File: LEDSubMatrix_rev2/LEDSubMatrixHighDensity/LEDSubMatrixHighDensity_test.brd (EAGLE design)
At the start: 16.9 x 146 mm, 145 parts, among them IC1 TLC5955DCAR, IC2 TLC5955DCAR, IC3 TLC5955DCAR, IC4 TLC5955DCAR, IC5 TLC5955DCAR, IC6 TLC5955DCAR, IC7 TLC5955DCAR, IC8 TLC5955DCAR

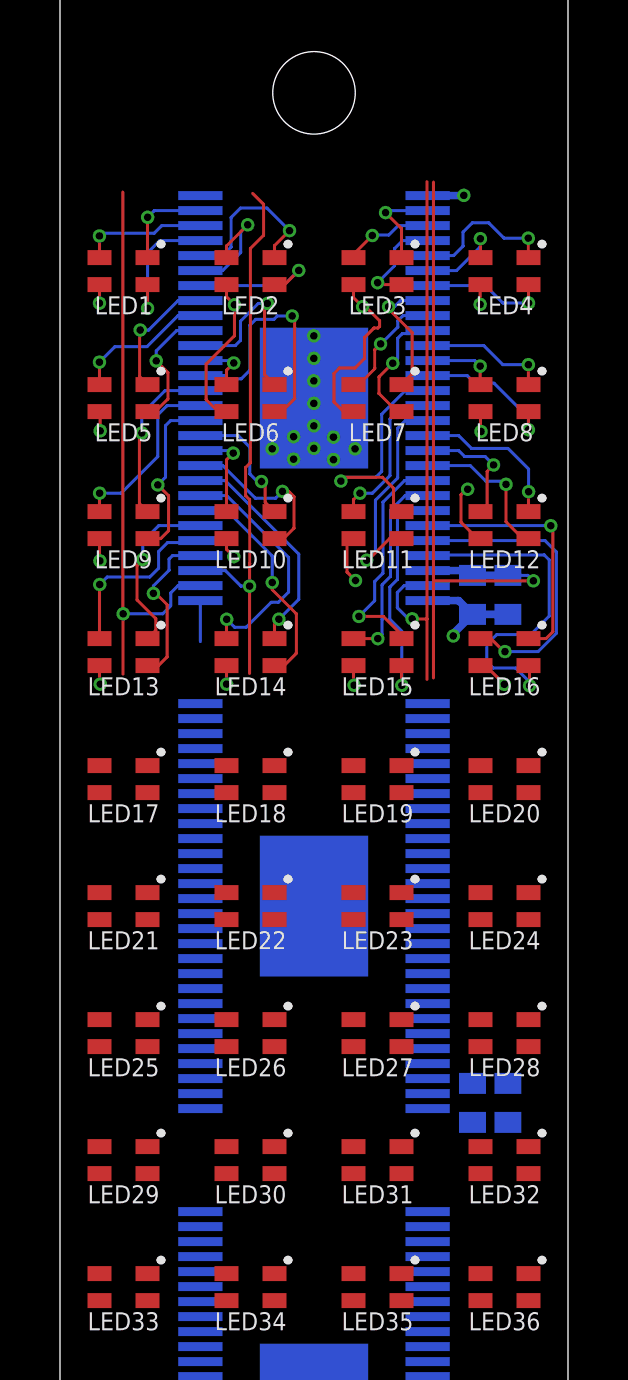
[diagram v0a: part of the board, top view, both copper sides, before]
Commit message: finished rev 2 of PCB submatrix led
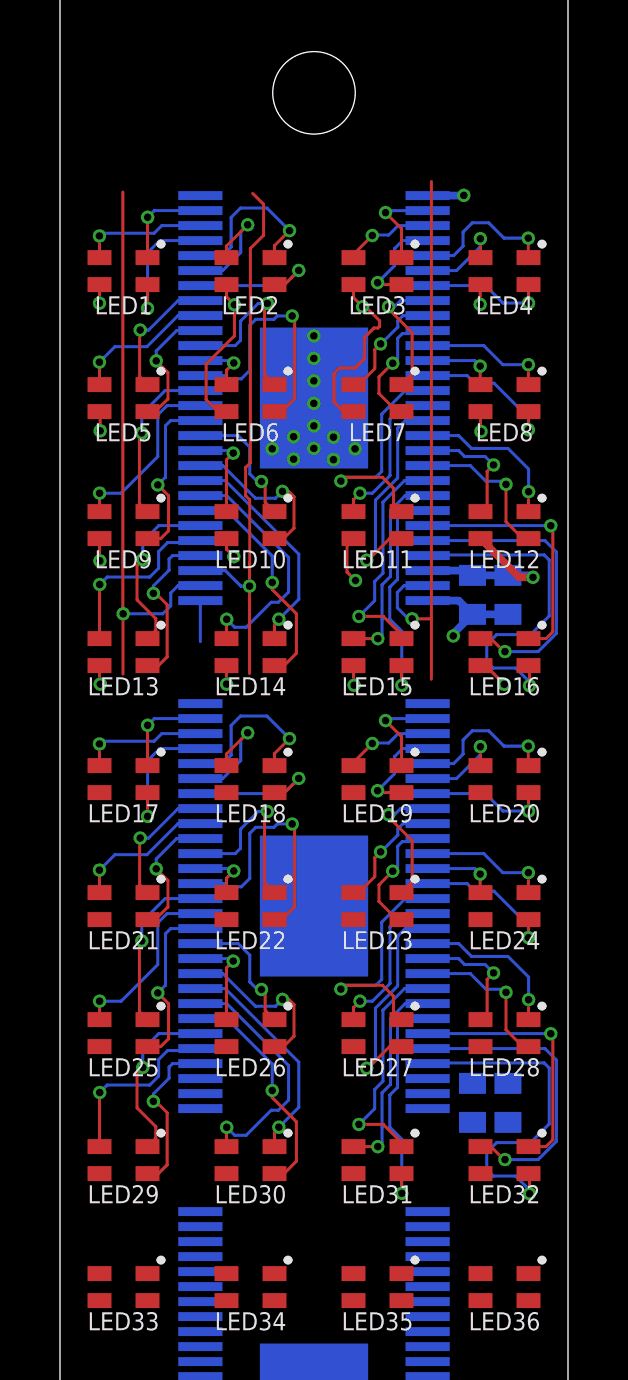
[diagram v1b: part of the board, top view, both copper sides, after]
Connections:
- removed net 3V3_LOGIC: C1.1, C1B.1, C2.1, C2B.1, C3.1, C3B.1, C4.1, C4B.1, C5.1, C5B.1, C6.1, C6B.1, C7.1, C7B.1, C8.1, C8B.1, IC1.54, IC2.54, IC3.54, IC4.54, IC5.54, IC6.54, IC7.54, IC8.54, SV1.9
- net 3V3: now also C1.1, C1B.1, C2.1, C2B.1, C3.1, C3B.1, C4.1, C4B.1, C5.1, C5B.1, C6.1, C6B.1, C7.1, C7B.1, C8.1, C8B.1, IC1.54, IC2.54, IC3.54, IC4.54, IC5.54, IC6.54, IC7.54, IC8.54
- net GND: now also SV1.9
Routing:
- net 3V3_LOGIC: track 23.5 -> 0.00 mm, vias 1 -> 0
- net N$LEDB32: track 0.00 -> 11.6 mm, vias 0 -> 1
- net N$LEDR32: track 0.00 -> 10.1 mm, vias 0 -> 1
- net N$LEDG32: track 0.00 -> 8.57 mm, vias 0 -> 1
- net N$LEDB22: track 0.00 -> 8.49 mm, vias 0 -> 1
- net N$LEDR30: track 0.00 -> 8.25 mm, vias 0 -> 1
- net N$LEDG27: track 0.00 -> 8.10 mm, vias 0 -> 1
- net N$LEDG31: track 0.00 -> 7.73 mm, vias 0 -> 1
- net N$LEDB31: track 0.00 -> 7.62 mm, vias 0 -> 1
- net N$LEDB30: track 0.00 -> 7.50 mm, vias 0 -> 1
- net N$LEDG30: track 0.00 -> 7.45 mm, vias 0 -> 1
- net N$LEDB27: track 0.00 -> 7.39 mm, vias 0 -> 1
- net N$LEDR31: track 0.00 -> 6.70 mm, vias 0 -> 1
- net N$LEDR29: track 0.00 -> 6.09 mm, vias 0 -> 1
- net N$LEDG22: track 0.00 -> 6.07 mm, vias 0 -> 1
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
